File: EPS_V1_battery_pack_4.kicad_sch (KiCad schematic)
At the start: 33 parts, among them U1 MP2672AGD-0000-Z, U5 MAX17205G+

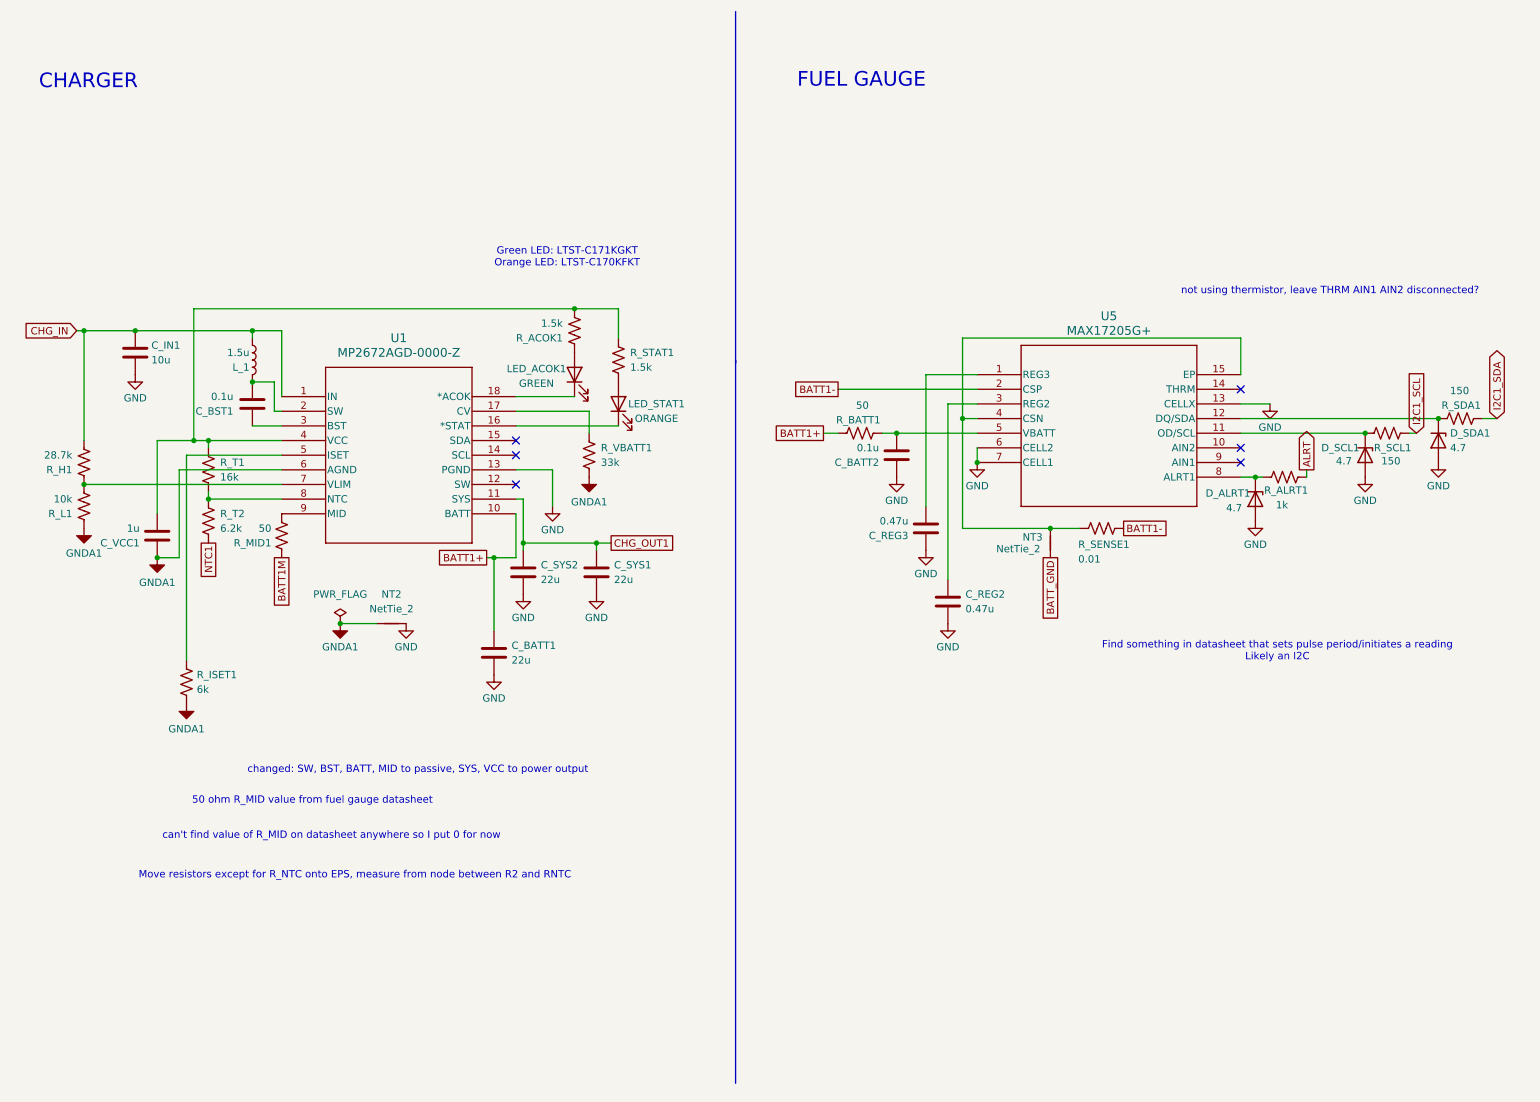
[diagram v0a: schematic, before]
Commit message: Add other battery packs, connect all ALRT signals, assign footprints for new components, make inhibit switch footprints
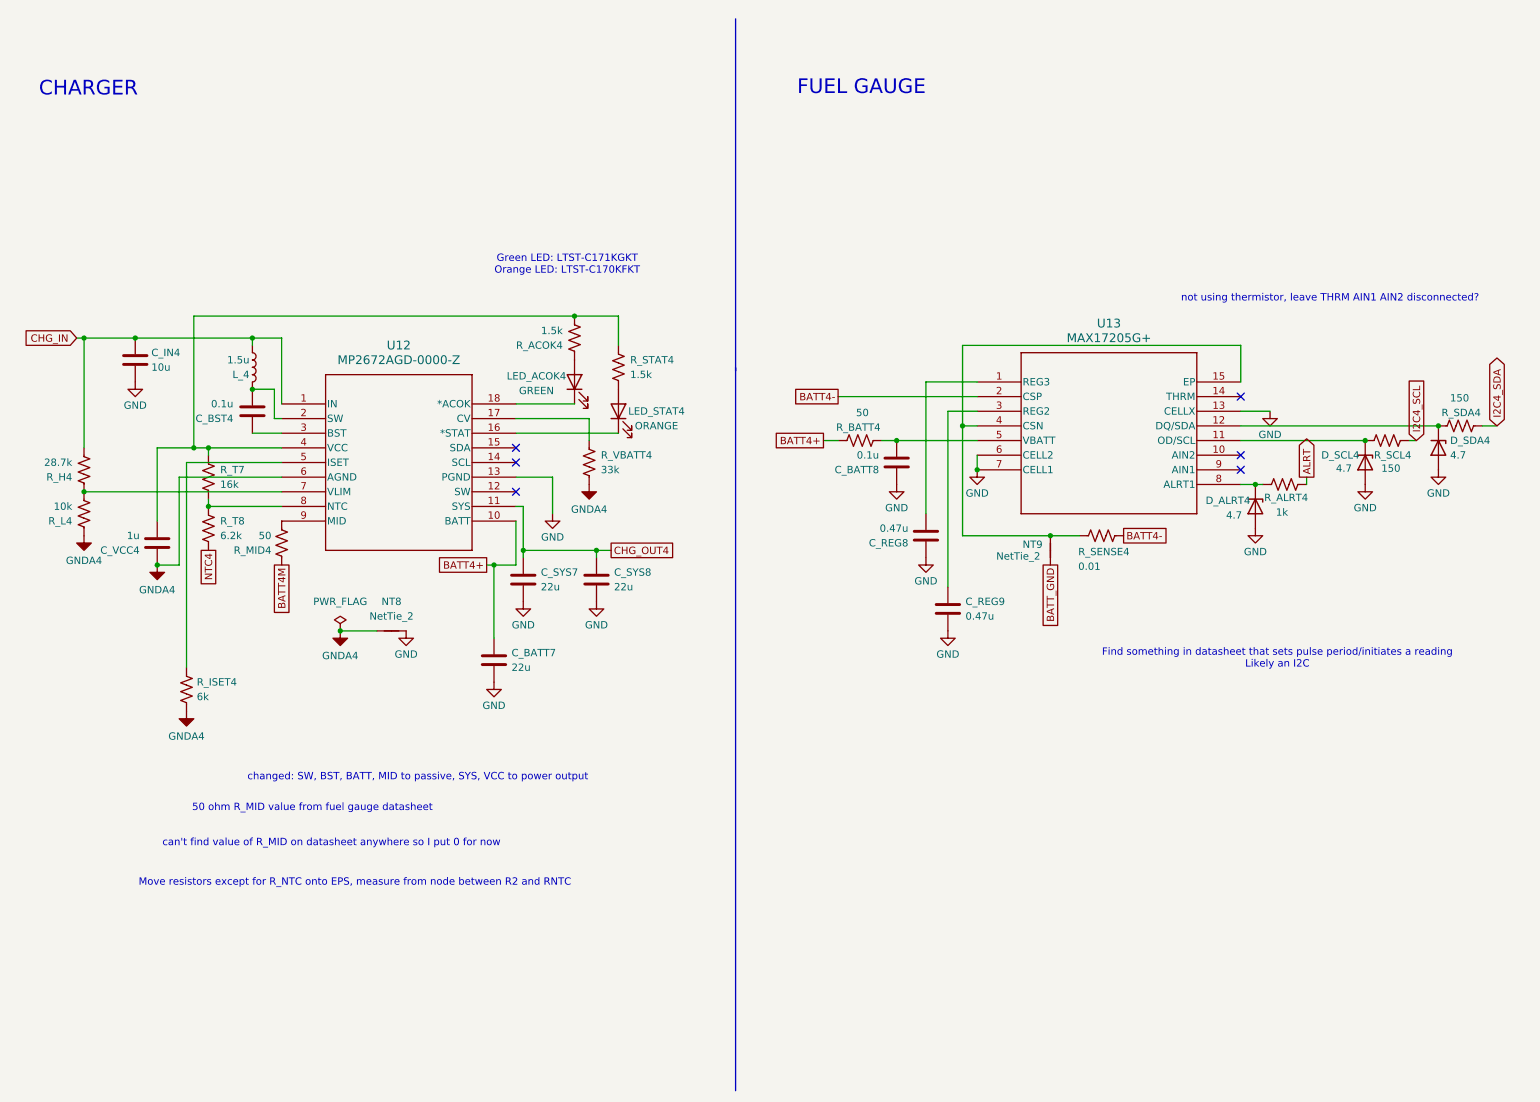
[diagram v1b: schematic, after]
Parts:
- removed C_BATT1, C_SYS1, C_SYS2: 22u, Capacitor_SMD:C_0805_2012Metric, symbol Device:C
- removed C_BATT2, C_BST1: 0.1u, Capacitor_SMD:C_0603_1608Metric, symbol Device:C
- removed C_IN1: 10u, Capacitor_SMD:C_0805_2012Metric, symbol Device:C
- removed C_REG2, C_REG3: 0.47u, Capacitor_SMD:C_0603_1608Metric, symbol Device:C
- removed C_VCC1: 1u, Capacitor_SMD:C_0603_1608Metric, symbol Device:C
- removed D_ALRT1, D_SCL1, D_SDA1: 4.7, Diode_SMD:D_0603_1608Metric, symbol Device:D_Zener
- removed LED_ACOK1: GREEN, LED_SMD:LED_0805_2012Metric, symbol Device:LED
- removed LED_STAT1: ORANGE, LED_SMD:LED_0805_2012Metric, symbol Device:LED
- removed L_1: 1.5u, AMELA2012S_1R5MT:IND_AMELA2012S-1R5MT, symbol Device:L
- removed NT2, NT3: NetTie_2, NetTie:NetTie-2_SMD_Pad2.0mm, symbol Device:NetTie_2
- removed R_ACOK1, R_STAT1: 1.5k, Resistor_SMD:R_0603_1608Metric, symbol Device:R_US
- removed R_ALRT1: 1k, Resistor_SMD:R_0603_1608Metric, symbol Device:R_US
- removed R_BATT1, R_MID1: 50, Resistor_SMD:R_0603_1608Metric, symbol Device:R_US
- removed R_H1: 28.7k, Resistor_SMD:R_0603_1608Metric, symbol Device:R_US
- removed R_ISET1: 6k, Resistor_SMD:R_0603_1608Metric, symbol Device:R_US
- removed R_L1: 10k, Resistor_SMD:R_0603_1608Metric, symbol Device:R_US
- removed R_SCL1, R_SDA1: 150, Resistor_SMD:R_0603_1608Metric, symbol Device:R_US
- removed R_SENSE1: 0.01, Resistor_SMD:R_0603_1608Metric, symbol Device:R_US
- removed R_T1: 16k, Resistor_SMD:R_0603_1608Metric, symbol Device:R_US
- removed R_T2: 6.2k, Resistor_SMD:R_0603_1608Metric, symbol Device:R_US
- removed R_VBATT1: 33k, Resistor_SMD:R_0603_1608Metric, symbol Device:R_US
- removed U1: MP2672AGD-0000-Z, MP2672AGD_0000_Z:QFN-18_MP2672A_MNP, symbol 2026-04-14_17-23-40:MP2672AGD-0000-Z
- removed U5: MAX17205G+, MAX17205G:21-0137_T1433&plus_2C_MXM, symbol MAX17205G:MAX17205G+
- added C_BATT7, C_SYS7, C_SYS8: 22u, Capacitor_SMD:C_0805_2012Metric, symbol Device:C
- added C_BATT8, C_BST4: 0.1u, Capacitor_SMD:C_0603_1608Metric, symbol Device:C
- added C_IN4: 10u, Capacitor_SMD:C_0805_2012Metric, symbol Device:C
- added C_REG8, C_REG9: 0.47u, Capacitor_SMD:C_0603_1608Metric, symbol Device:C
- added C_VCC4: 1u, Capacitor_SMD:C_0603_1608Metric, symbol Device:C
- added D_ALRT4, D_SCL4, D_SDA4: 4.7, Diode_SMD:D_0603_1608Metric, symbol Device:D_Zener
- added LED_ACOK4: GREEN, LED_SMD:LED_0805_2012Metric, symbol Device:LED
- added LED_STAT4: ORANGE, LED_SMD:LED_0805_2012Metric, symbol Device:LED
- added L_4: 1.5u, AMELA2012S_1R5MT:IND_AMELA2012S-1R5MT, symbol Device:L
- added NT8, NT9: NetTie_2, NetTie:NetTie-2_SMD_Pad2.0mm, symbol Device:NetTie_2
- added R_ACOK4, R_STAT4: 1.5k, Resistor_SMD:R_0603_1608Metric, symbol Device:R_US
- added R_ALRT4: 1k, Resistor_SMD:R_0603_1608Metric, symbol Device:R_US
- added R_BATT4, R_MID4: 50, Resistor_SMD:R_0603_1608Metric, symbol Device:R_US
- added R_H4: 28.7k, Resistor_SMD:R_0603_1608Metric, symbol Device:R_US
- added R_ISET4: 6k, Resistor_SMD:R_0603_1608Metric, symbol Device:R_US
- added R_L4: 10k, Resistor_SMD:R_0603_1608Metric, symbol Device:R_US
- added R_SCL4, R_SDA4: 150, Resistor_SMD:R_0603_1608Metric, symbol Device:R_US
- added R_SENSE4: 0.01, Resistor_SMD:R_0603_1608Metric, symbol Device:R_US
- added R_T7: 16k, Resistor_SMD:R_0603_1608Metric, symbol Device:R_US
- added R_T8: 6.2k, Resistor_SMD:R_0603_1608Metric, symbol Device:R_US
- added R_VBATT4: 33k, Resistor_SMD:R_0603_1608Metric, symbol Device:R_US
- added U12: MP2672AGD-0000-Z, MP2672AGD_0000_Z:QFN-18_MP2672A_MNP, symbol 2026-04-14_17-23-40:MP2672AGD-0000-Z
- added U13: MAX17205G+, MAX17205G:21-0137_T1433&plus_2C_MXM, symbol MAX17205G:MAX17205G+
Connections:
- net ALRT: now also R_ALRT4.2
- net BATT_GND: now also NT9.1
- net CHG_IN: now also C_IN4.1, L_4.1, R_H4.2, U12.1 (IN)
- net GND: now also C_BATT7.2, C_BATT8.1, C_IN4.2, C_REG8.1, C_REG9.2, C_SYS7.2, C_SYS8.2, D_ALRT4.2 (A), D_SCL4.2 (A), D_SDA4.2 (A), NT8.2, U12.13 (PGND), U13.13 (CELLX), U13.6 (CELL2), U13.7 (CELL1)
- new net: D_ALRT4.1 (K), R_ALRT4.1, U13.8 (ALRT1)
- new net: D_SDA4.1 (K), R_SDA4.1, U13.12 (DQ/SDA)
- new net: C_BST4.2, L_4.2, U12.2 (SW)
- new net: R_H4.1, R_L4.2, U12.7 (VLIM)
- new net: R_T7.2, R_T8.1, U12.8 (NTC)
- new net: D_SCL4.1 (K), R_SCL4.1, U13.11 (OD/SCL)
- new net: LED_STAT4.1 (K), U12.16 (*STAT)
- new net: LED_STAT4.2 (A), R_STAT4.2
- new net: NT9.2, R_SENSE4.2, U13.15 (EP), U13.4 (CSN)
- new net: C_BATT8.2, R_BATT4.2, U13.5 (VBATT)
- new net: C_REG8.2, U13.1 (REG3)
- new net: R_ISET4.1, U12.5 (ISET)
- new net: LED_ACOK4.2 (A), R_ACOK4.1
- new net: C_VCC4.2, R_ACOK4.2, R_STAT4.1, R_T7.1, U12.4 (VCC)
- new net: R_MID4.2, U12.9 (MID)
- new net: R_VBATT4.1, U12.17 (CV)
- new net: LED_ACOK4.1 (K), U12.18 (*ACOK)
- new net: C_REG9.1, U13.3 (REG2)
- new net: C_BST4.1, U12.3 (BST)
- new net BATT4+: C_BATT7.1, R_BATT4.1, U12.10 (BATT)
- new net BATT4-: R_SENSE4.1, U13.2 (CSP)
- new net BATT4M: R_MID4.1
- new net CHG_OUT4: C_SYS7.1, C_SYS8.1, U12.11 (SYS)
- new net GNDA4: C_VCC4.1, NT8.1, R_ISET4.2, R_L4.1, R_VBATT4.2, U12.6 (AGND)
- new net I2C4_SCL: R_SCL4.2
- new net I2C4_SDA: R_SDA4.2
- new net NTC4: R_T8.2

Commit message: Do layout draft
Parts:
- removed D_ALRT4: 4.7, Diode_SMD:D_0603_1608Metric, symbol Device:D_Zener
- removed R_ALRT4: 1k, Resistor_SMD:R_0603_1608Metric, symbol Device:R_US
- NT8, NT9: footprint NetTie:NetTie-2_SMD_Pad2.0mm -> NetTie:NetTie-2_SMD_Pad0.5mm
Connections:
- net ALRT: now also U13.8 (ALRT1)
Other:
- moved on the sheet: D_SCL4, D_SDA4, R_SCL4, R_SDA4
